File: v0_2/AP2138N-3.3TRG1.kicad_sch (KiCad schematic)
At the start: 4 parts, among them IC3 AP2138N-3.3TRG1, Q1 DMG2301L-7, Q2 DMG2301L-7, Q4 DMN3731U-7

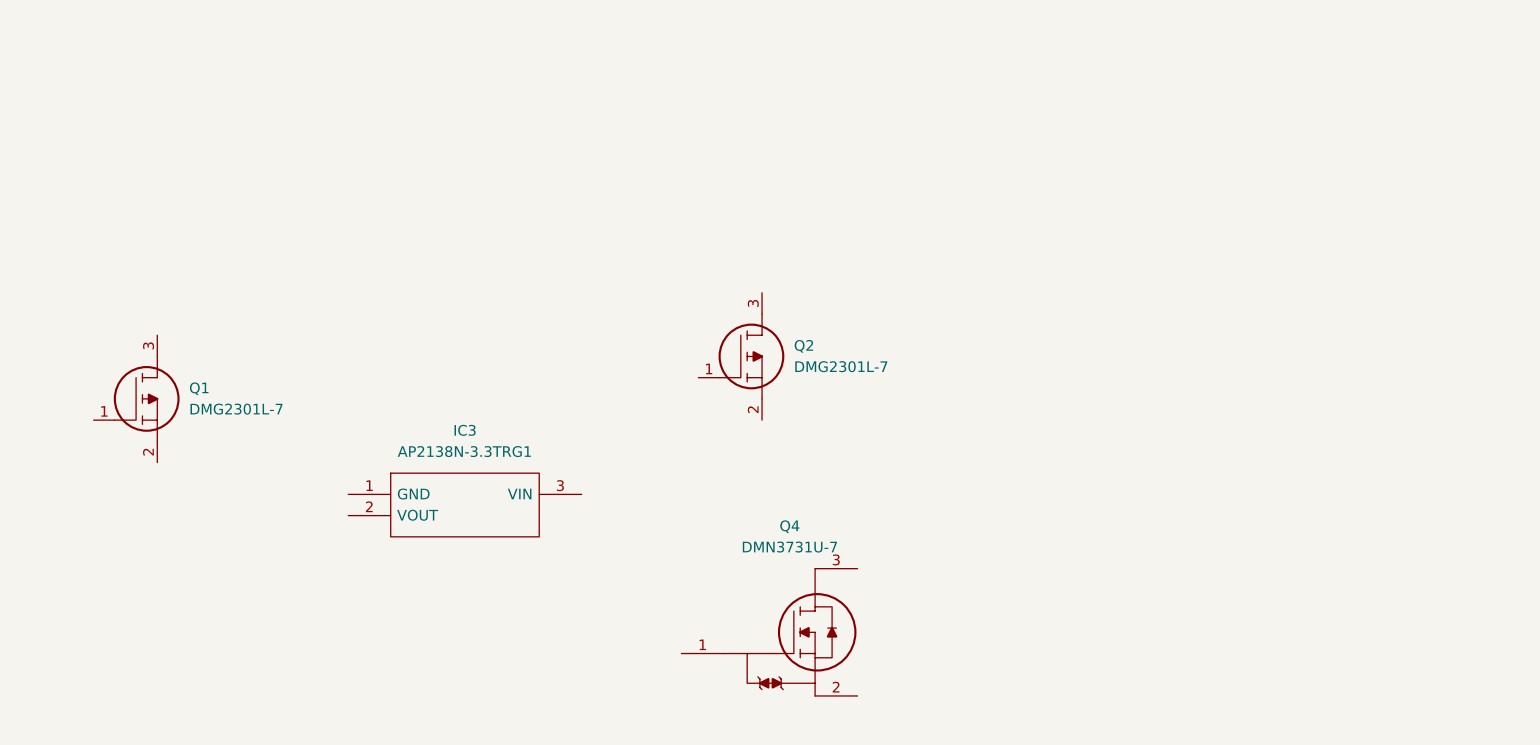
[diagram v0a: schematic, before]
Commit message: add sensor schematic
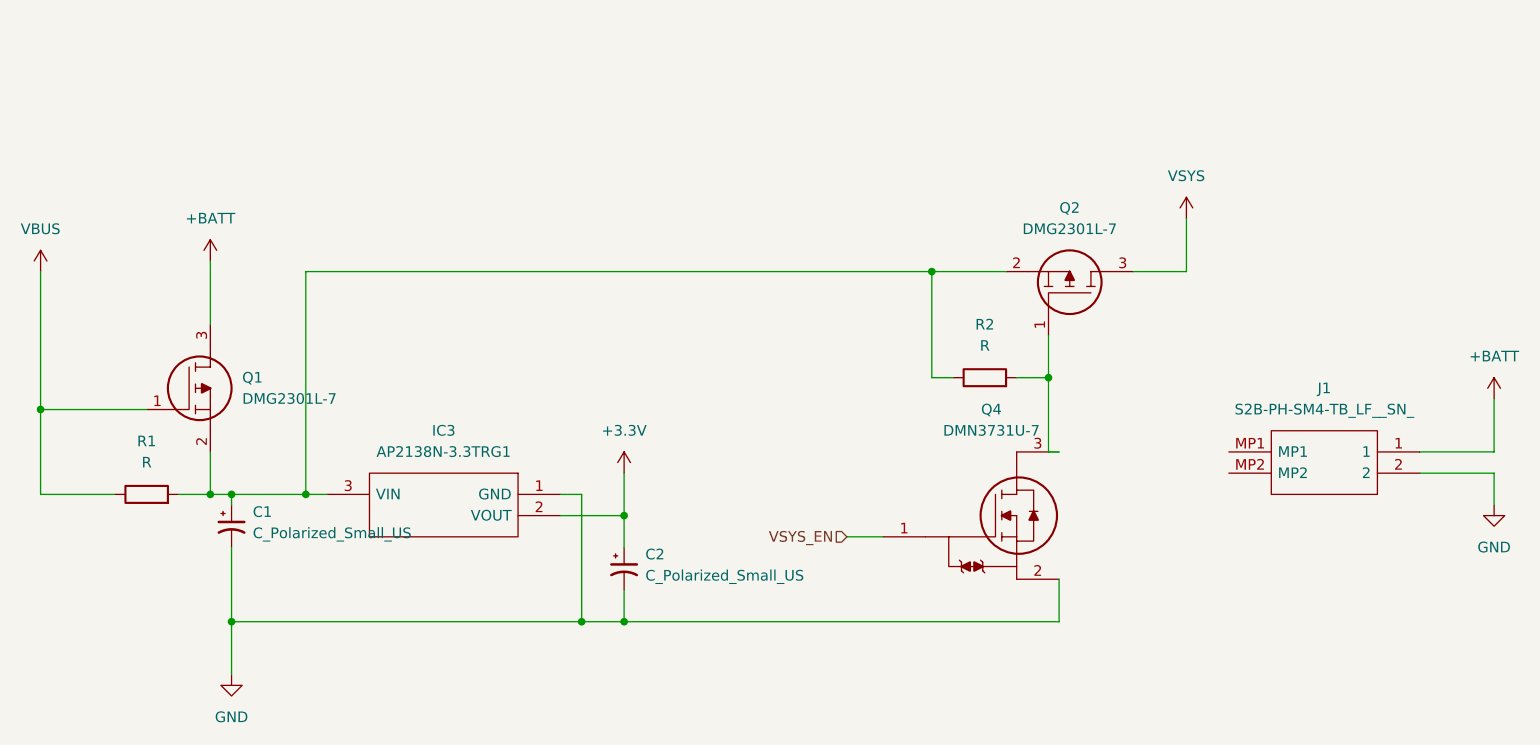
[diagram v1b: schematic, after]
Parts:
- added C1, C2: C_Polarized_Small_US, symbol Device:C_Polarized_Small_US
- added J1: S2B-PH-SM4-TB_LF__SN_, S2BPHSM4TBLFSN, symbol S2B-PH-SM4-TB_LF__SN_:S2B-PH-SM4-TB_LF__SN_
- added R1, R2: R, symbol Device:R
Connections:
- net at Q2.1: now also Q4.3, R2.2
- net at Q2.2: now also IC3.3 (VIN), Q1.2, C1.1, R1.2, R2.1
- net VSYS: now reaches Q2.3
- net VSYS_EN: now reaches Q4.1
- net GND: now reaches Q4.2
- net GND: now also IC3.1 (GND), C1.2, C2.2, J1.2
- net VBUS: now reaches Q1.1
- net VBUS: now also R1.1
- net +BATT: now reaches Q1.3
- net +BATT: now also J1.1
- net +3.3V: now reaches IC3.2 (VOUT)
- net +3.3V: now also C2.1
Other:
- moved on the sheet: IC3, Q1, Q2, Q4

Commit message: schematic for enviro done
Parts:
- removed Q4: DMN3731U-7, SOT96P240X110-3N, symbol DMN3731U-7:DMN3731U-7
- added Q4: DMN3731U-13, symbol DMN3731U-13:DMN3731U-13
- J1: footprint S2BPHSM4TBLFSN -> S2B-PH-SM4-TB(LF)(SN):S2BPHSM4TBLFSN
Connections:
- net GND: now also Q4.2
- net VSYS_EN: now also Q4.1
- net at Q2.1, R2.2: now also Q4.3
- net +3.3V renamed V+_A0
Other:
- note added: "LDO"
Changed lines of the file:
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@@
   (junction (at 110.49 90.17) (diameter 0) (color 0 0 0 0)
   )
+  (junction (at 148.59 88.9) (diameter 0) (color 0 0 0 0)
+  )
   (junction (at 78.74 80.01) (diameter 0) (color 0 0 0 0)
   )
@@
     (stroke (width 0) (type default))
   )
-  (wire (pts (xy 175.26 95.25) (xy 179.578 95.25))
+  (wire (pts (xy 187.96 95.25) (xy 193.04 95.25))
     (stroke (width 0) (type default))
   )
@@
     (stroke (width 0) (type default))
   )
+  (wire (pts (xy 148.59 88.9) (xy 152.4 88.9))
+    (stroke (width 0) (type default))
+  )
   (wire (pts (xy 140.97 92.71) (xy 148.59 92.71))
     (stroke (width 0) (type default))
@@
     (stroke (width 0) (type default))
   )
-  (wire (pts (xy 148.59 92.71) (xy 148.59 87.63))
+  (wire (pts (xy 148.59 92.71) (xy 148.59 88.9))
     (stroke (width 0) (type default))
   )
@@
     (stroke (width 0) (type default))
   )
+  (wire (pts (xy 148.59 88.9) (xy 148.59 87.63))
+    (stroke (width 0) (type default))
+  )
   (wire (pts (xy 187.96 76.2) (xy 185.42 76.2))
     (stroke (width 0) (type default))
@@
     (stroke (width 0) (type default))
   )
-  (hierarchical_label "VSYS_EN" (shape input) (at 175.26 95.25 180) (fields_autoplaced)
+  (text "LDO" (at 78.74 38.1 0)
+    (effects (font (face "Ubuntu") (size 3 3) (thickness 1) bold) (justify left bottom))
+  )
+  (hierarchical_label "VSYS_EN" (shape input) (at 187.96 95.25 180) (fields_autoplaced)
     (effects (font (size 1.27 1.27)) (justify right))
+  )
+  (hierarchical_label "V+_A0" (shape input) (at 152.4 88.9 0) (fields_autoplaced)
+    (effects (font (size 1.27 1.27)) (justify left))
   )
   (symbol (lib_id "Device:C_Polarized_Small_US") (at 101.6 93.98 0) (unit 1)
@@
     )
   )
+  (symbol (lib_id "power_vsys:V+_A0") (at 148.59 87.63 0) (unit 1)
+    (in_bom yes) (on_board yes) (dnp no) (fields_autoplaced)
+    (property "Reference" "#PWR04" (at 148.59 91.44 0)
+      (effects (font (size 1.27 1.27)) hide)
+    )
+    (property "Value" "V+_A0" (at 148.59 82.55 0)
+      (effects (font (size 1.27 1.27)))
+    )
+    (property "Footprint" "" (at 148.59 87.63 0)
+      (effects (font (size 1.27 1.27)) hide)
+    )
+    (property "Datasheet" "" (at 148.59 87.63 0)
+      (effects (font (size 1.27 1.27)) hide)
+    )
+    (pin "1")
+    (instances
+      (project "v0_2"
+        (path "/678523e5-508b-4706-b0e0-f17e466a8d09/3580e7c3-86d9-4e19-aad4-f7334a732566"
+          (reference "#PWR04") (unit 1)
+        )
+      )
+    )
+  )
+  (symbol (lib_id "DMN3731U-13:DMN3731U-13") (at 193.04 95.25 0) (unit 1)
+    (in_bom yes) (on_board yes) (dnp no) (fields_autoplaced)
+    (property "Reference" "Q4" (at 204.47 91.44 0)
+      (effects (font (size 1.27 1.27)) (justify left))
+    )
+    (property "Value" "DMN3731U-13" (at 204.47 93.98 0)
+      (effects (font (size 1.27 1.27)) (justify left))
+    )
+    (property "Footprint" "" (at 204.47 96.52 0)
+      (effects (font (size 1.27 1.27)) (justify left) hide)
+    )
+    (property "Datasheet" "https://www.diodes.com/assets/Datasheets/DMN3731U.pdf" (at 204.47 99.06 0)
+      (effects (font (size 1.27 1.27)) (justify left) hide)
+    )
+    (property "Description" "MOSFET MOSFET BVDSS: 25V-30V" (at 204.47 101.6 0)
+      (effects (font (size 1.27 1.27)) (justify left) hide)
+    )
+    (property "Height" "1.1" (at 204.47 104.14 0)
+      (effects (font (size 1.27 1.27)) (justify left) hide)
+    )
+    (property "Manufacturer_Name" "Diodes Inc." (at 204.47 106.68 0)
+      (effects (font (size 1.27 1.27)) (justify left) hide)
+    )
+    (property "Manufacturer_Part_Number" "DMN3731U-13" (at 204.47 109.22 0)
+      (effects (font (size 1.27 1.27)) (justify left) hide)
+    )
+    (property "Mouser Part Number" "621-DMN3731U-13" (at 204.47 111.76 0)
+      (effects (font (size 1.27 1.27)) (justify left) hide)
+    )
+    (property "Mouser Price/Stock" "https://www.mouser.co.uk/ProductDetail/Diodes-Incorporated/DMN3731U-13?qs=EBDBlbfErPwOKX9Ga5s0uA%3D%3D" (at 204.47 114.3 0)
+      (effects (font (size 1.27 1.27)) (justify left) hide)
+    )
+    (property "Arrow Part Number" "" (at 204.47 116.84 0)
+      (effects (font (size 1.27 1.27)) (justify left) hide)
+    )
+    (property "Arrow Price/Stock" "" (at 204.47 119.38 0)
+      (effects (font (size 1.27 1.27)) (justify left) hide)
+    )
+    (pin "1")
+    (pin "2")
+    (pin "3")
+    (instances
+      (project "v0_2"
+        (path "/678523e5-508b-4706-b0e0-f17e466a8d09/3580e7c3-86d9-4e19-aad4-f7334a732566"
+          (reference "Q4") (unit 1)
+        )
+      )
+    )
+  )
   (symbol (lib_id "Device:R") (at 91.44 90.17 90) (unit 1)
     (in_bom yes) (on_board yes) (dnp no)
@@
     )
   )
-  (symbol (lib_id "DMN3731U-7:DMN3731U-7") (at 187.96 95.25 0) (unit 1)
-    (in_bom yes) (on_board yes) (dnp no) (fields_autoplaced)
-    (property "Reference" "Q4" (at 192.5574 80.01 0)
-      (effects (font (size 1.27 1.27)))
-    )
-    (property "Value" "DMN3731U-7" (at 192.5574 82.55 0)
-      (effects (font (size 1.27 1.27)))
-    )
-    (property "Footprint" "SOT96P240X110-3N" (at 202.692 76.2 0)
-      (effects (font (size 1.27 1.27)) (justify left) hide)
-    )
-    (property "Datasheet" "https://www.mouser.fr/datasheet/2/115/DMN3731U-1594715.pdf" (at 202.692 78.74 0)
-      (effects (font (size 1.27 1.27)) (justify left) hide)
-    )
-    (property "Description" "MOSFET MOSFET BVDSS: 25V-30V" (at 202.692 81.28 0)
-      (effects (font (size 1.27 1.27)) (justify left) hide)
-    )
-    (property "Height" "1.1" (at 202.692 83.82 0)
-      (effects (font (size 1.27 1.27)) (justify left) hide)
-    )
-    (property "Manufacturer_Name" "Diodes Inc." (at 202.692 86.36 0)
-      (effects (font (size 1.27 1.27)) (justify left) hide)
-    )
-    (property "Manufacturer_Part_Number" "DMN3731U-7" (at 202.692 88.9 0)
-      (effects (font (size 1.27 1.27)) (justify left) hide)
-    )
-    (property "Mouser Part Number" "621-DMN3731U-7" (at 202.692 91.44 0)
-      (effects (font (size 1.27 1.27)) (justify left) hide)
-    )
-    (property "Mouser Price/Stock" "https://www.mouser.co.uk/ProductDetail/Diodes-Incorporated/DMN3731U-7?qs=EBDBlbfErPyEqvOCBrONHQ%3D%3D" (at 202.692 93.98 0)
-      (effects (font (size 1.27 1.27)) (justify left) hide)
-    )
-    (property "Arrow Part Number" "" (at 202.692 96.52 0)
-      (effects (font (size 1.27 1.27)) (justify left) hide)
-    )
-    (property "Arrow Price/Stock" "" (at 202.692 99.06 0)
-      (effects (font (size 1.27 1.27)) (justify left) hide)
-    )
-    (pin "1")
-    (pin "2")
-    (pin "3")
-    (instances
-      (project "v0_2"
-        (path "/678523e5-508b-4706-b0e0-f17e466a8d09/3580e7c3-86d9-4e19-aad4-f7334a732566"
-          (reference "Q4") (unit 1)
-        )
-      )
-    )
-  )
-  (symbol (lib_id "power:+3.3V") (at 148.59 87.63 0) (unit 1)
-    (in_bom yes) (on_board yes) (dnp no) (fields_autoplaced)
-    (property "Reference" "#PWR04" (at 148.59 91.44 0)
-      (effects (font (size 1.27 1.27)) hide)
-    )
-    (property "Value" "+3.3V" (at 148.59 82.55 0)
-      (effects (font (size 1.27 1.27)))
-    )
-    (property "Footprint" "" (at 148.59 87.63 0)
-      (effects (font (size 1.27 1.27)) hide)
-    )
-    (property "Datasheet" "" (at 148.59 87.63 0)
-      (effects (font (size 1.27 1.27)) hide)
-    )
-    (pin "1")
-    (instances
-      (project "v0_2"
-        (path "/678523e5-508b-4706-b0e0-f17e466a8d09/3580e7c3-86d9-4e19-aad4-f7334a732566"
-          (reference "#PWR04") (unit 1)
-        )
-      )
-    )
-  )
   (symbol (lib_id "S2B-PH-SM4-TB_LF__SN_:S2B-PH-SM4-TB_LF__SN_") (at 243.84 87.63 180) (unit 1)
     (in_bom yes) (on_board yes) (dnp no) (fields_autoplaced)
@@
       (effects (font (size 1.27 1.27)))
     )
-    (property "Footprint" "S2BPHSM4TBLFSN" (at 224.79 90.17 0)
-      (effects (font (size 1.27 1.27)) (justify left) hide)
-    )
+    (property "Footprint" "S2B-PH-SM4-TB(LF)(SN):S2BPHSM4TBLFSN" (at 224.79 90.17 0)
+      (effects (font (size 1.27 1.27)) (justify left) hide)
+    )

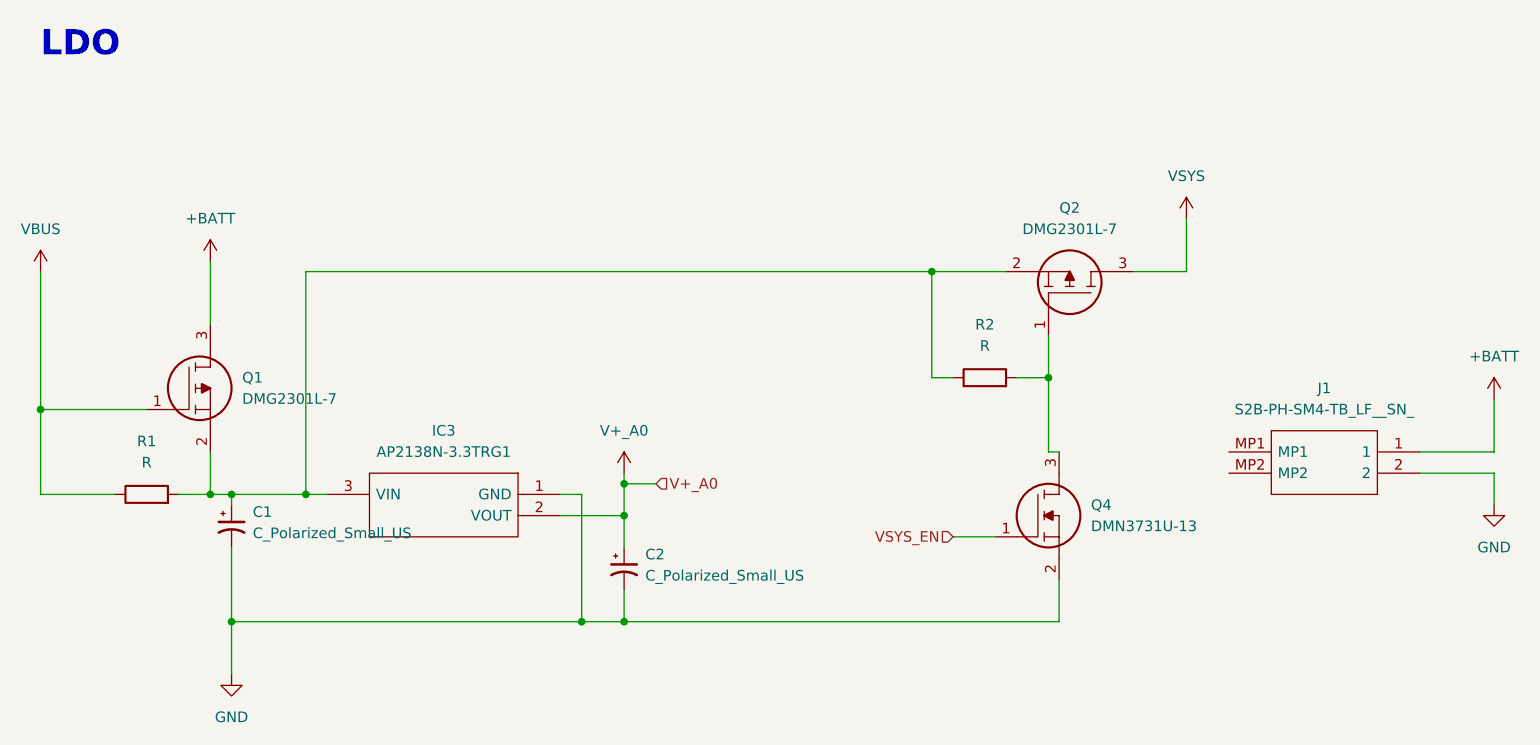
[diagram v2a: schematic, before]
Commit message: all part are added
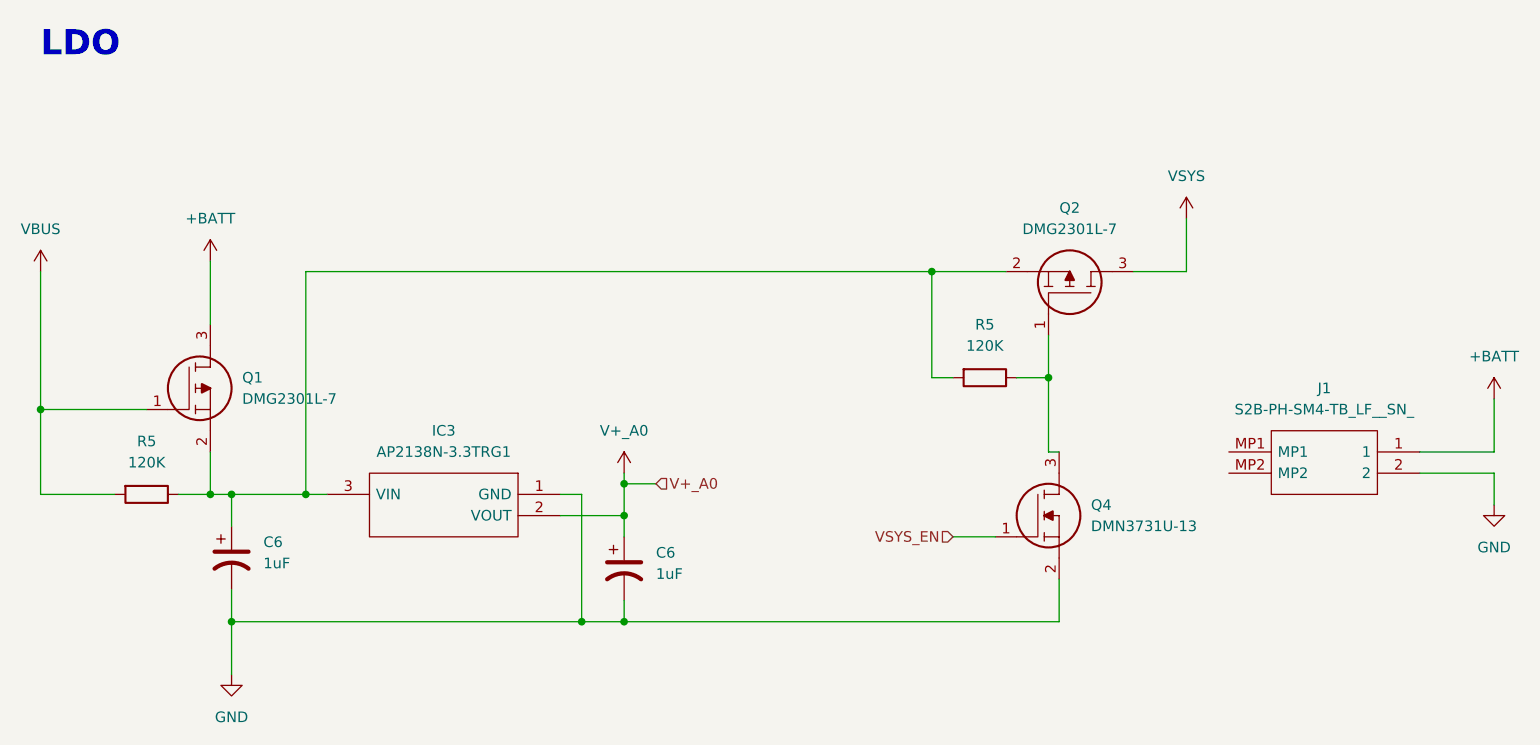
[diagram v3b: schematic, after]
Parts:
- removed C1, C2: C_Polarized_Small_US, symbol Device:C_Polarized_Small_US
- removed R1, R2: R, symbol Device:R
- added C6 (x2): 1uF, Capacitor_SMD:C_0603_1608Metric, symbol Device:C_Polarized_US
- added R5 (x2): 120K, Resistor_SMD:R_0603_1608Metric, symbol Device:R
- Q4: footprint (none) -> DMN3731U-13:SOT96P240X110-3N
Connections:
- net GND: now also C6.2, C6.2
- net V+_A0: now also C6.1
- net VBUS: now also R5.2
- net at IC3.3 (VIN), Q1.2, Q2.2: now also C6.1, R5.1, R5.2
- net at Q2.1, Q4.3: now also R5.1
